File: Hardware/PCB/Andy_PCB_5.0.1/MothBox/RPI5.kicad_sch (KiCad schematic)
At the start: 4 parts, among them U4 RASPBERRY_PI_4B_4GB, U5 RASPBERRY_PI_5, U6 RASPBERRY_PI_4B_4GB, U7 Female Inv Socket Pi 2.54-2*20

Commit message: daily schematic updates
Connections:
- net +3.3V: now also U5.17 (3V3)
- net COM_I/O: no longer names the net of U7.35
- net EN_MUX1 renamed UV2_CTRL
- net EN_MUX2 renamed UV3_CTRL
- net L_LED_CTRL renamed PHOTO_LED_CTRL
- net S0_MUX: no longer names the net of U7.34
- net S1_MUX: no longer names the net of U7.14
- net S2_MUX: no longer names the net of U7.11
- net S3_MUX: no longer names the net of U7.16
- no-connect marks 20 -> 24

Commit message: updated photo LEDs and the power page
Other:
- company: (none) -> Digital Naturalism Laboritories
- title: (none) -> MothBox
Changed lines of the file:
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@@
 	(generator_version "9.0")
 	(paper "User" 381 254)
+	(title_block
+		(title "MothBox")
+		(date "2025-07-12")
+		(rev "5.0.1")
+		(company "Digital Naturalism Laboritories")
+	)
 	(rectangle
 		(start 19.05 16.51)

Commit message: updated footprints and schematic
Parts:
- U4, U6: symbol MB_Library:RASPBERRY_PI_4B_4GB_1 -> MothBox_Symbol_Library:RASPBERRY_PI_4B_4GB_1; Digikey Part No SC1113 -> (none); Digikey_Part_No (none) -> SC1113
- U5: symbol MB_Library:RASPBERRY_PI_4B_4GB_2 -> MothBox_Symbol_Library:RASPBERRY_PI_4B_4GB_2; LCSC Part no  C5224014 -> (none); LCSC_Part_No (none) -> C5224014
- U7: footprint easyeda2kicad:HDR-TH_40P-P2.54-H-F-R2-C20-W8.5 -> easyeda_footprints:HDR-TH_40P-P2.54-H-F-R2-C20-W8.5; symbol MB_Library:2.54-2*20 -> MothBox_Symbol_Library:2.54-2*20; LCSC Part C2897440 -> (none); LCSC_Part (none) -> C2897440
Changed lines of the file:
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@@
 	(symbol
 		(lib_name "RASPBERRY_PI_4B_4GB_1")
-		(lib_id "MB_Library:RASPBERRY_PI_4B_4GB_1")
+		(lib_id "MothBox_Symbol_Library:RASPBERRY_PI_4B_4GB_1")
 		(at 102.87 173.99 0)
 		(unit 1)
@@
 			)
 		)
-		(property "Digikey Part No" "SC1113"
-			(at 102.87 173.99 0)
-			(effects
-				(font
-					(size 1.27 1.27)
-				)
-				(justify bottom)
-				(hide yes)
-			)
-		)
 		(property "Availability" "Not in stock"
 			(at 102.87 173.99 0)
@@
 			)
 		)
-		(property "LCSC PN" ""
-			(at 102.87 173.99 0)
-			(effects
-				(font
-					(size 1.27 1.27)
-				)
+		(property "AVAILABILITY" ""
+			(at 102.87 173.99 0)
+			(effects
+				(font
+					(size 1.27 1.27)
+				)
+				(hide yes)
+			)
+		)
+		(property "DESCRIPTION" ""
+			(at 102.87 173.99 0)
+			(effects
+				(font
+					(size 1.27 1.27)
+				)
+				(hide yes)
+			)
+		)
+		(property "Link" ""
+			(at 102.87 173.99 0)
+			(effects
+				(font
+					(size 1.27 1.27)
+				)
+				(hide yes)
+			)
+		)
+		(property "PACKAGE" ""
+			(at 102.87 173.99 0)
+			(effects
+				(font
+					(size 1.27 1.27)
+				)
+				(hide yes)
+			)
+		)
+		(property "PRICE" ""
+			(at 102.87 173.99 0)
+			(effects
+				(font
+					(size 1.27 1.27)
+				)
+				(hide yes)
+			)
+		)
+		(property "Digikey_Part_No" "SC1113"
+			(at 102.87 173.99 0)
+			(effects
+				(font
+					(size 1.27 1.27)
+				)
+				(hide yes)
 			)
 		)
@@
 	)
 	(symbol
-		(lib_id "MB_Library:GND")
+		(lib_id "MothBox_Symbol_Library:GND")
 		(at 137.16 111.76 0)
 		(unit 1)
@@
 	)
 	(symbol
-		(lib_id "MB_Library:GND")
+		(lib_id "MothBox_Symbol_Library:GND")
 		(at 97.79 124.46 0)
 		(unit 1)
@@
 	)
 	(symbol
-		(lib_id "MB_Library:+5V")
+		(lib_id "MothBox_Symbol_Library:+5V")
 		(at 97.79 39.37 0)
 		(unit 1)
@@
 	(symbol
 		(lib_name "RASPBERRY_PI_4B_4GB_2")
-		(lib_id "MB_Library:RASPBERRY_PI_4B_4GB_2")
+		(lib_id "MothBox_Symbol_Library:RASPBERRY_PI_4B_4GB_2")
 		(at 71.12 71.12 0)
 		(unit 1)
@@
 			)
 		)
-		(property "LCSC Part no " "C5224014"
+		(property "AVAILABILITY" ""
+			(at 71.12 71.12 0)
+			(effects
+				(font
+					(size 1.27 1.27)
+				)
+				(hide yes)
+			)
+		)
+		(property "DESCRIPTION" ""
+			(at 71.12 71.12 0)
+			(effects
+				(font
+					(size 1.27 1.27)
+				)
+				(hide yes)
+			)
+		)
+		(property "Link" ""
+			(at 71.12 71.12 0)
+			(effects
+				(font
+					(size 1.27 1.27)
+				)
+				(hide yes)
+			)
+		)
+		(property "PACKAGE" ""
+			(at 71.12 71.12 0)
+			(effects
+				(font
+					(size 1.27 1.27)
+				)
+				(hide yes)
+			)
+		)
+		(property "PRICE" ""
+			(at 71.12 71.12 0)
+			(effects
+				(font
+					(size 1.27 1.27)
+				)
+				(hide yes)
+			)
+		)
+		(property "LCSC_Part_No" "C5224014"
 			(at 71.12 71.12 0)
 			(effects
@@
 	)
 	(symbol
-		(lib_id "MB_Library:+3.3V")
+		(lib_id "MothBox_Symbol_Library:+3.3V")
 		(at 100.33 46.99 0)
 		(unit 1)
@@
 	)
 	(symbol
-		(lib_id "MB_Library:GND")
+		(lib_id "MothBox_Symbol_Library:GND")
 		(at 213.36 102.87 0)
 		(unit 1)
@@
 	(symbol
 		(lib_name "RASPBERRY_PI_4B_4GB_1")
-		(lib_id "MB_Library:RASPBERRY_PI_4B_4GB_1")
+		(lib_id "MothBox_Symbol_Library:RASPBERRY_PI_4B_4GB_1")
 		(at 64.77 172.72 0)
 		(unit 1)
@@
 			)
 		)
-		(property "Digikey Part No" "SC1113"
-			(at 64.77 172.72 0)
-			(effects
-				(font
-					(size 1.27 1.27)
-				)
-				(justify bottom)
-				(hide yes)
-			)
-		)
 		(property "Availability" "Not in stock"
 			(at 64.77 172.72 0)
@@
 			)
 		)
-		(property "LCSC PN" ""
-			(at 64.77 172.72 0)
-			(effects
-				(font
-					(size 1.27 1.27)
-				)
+		(property "AVAILABILITY" ""
+			(at 64.77 172.72 0)
+			(effects
+				(font
+					(size 1.27 1.27)
+				)
+				(hide yes)
+			)
+		)
+		(property "DESCRIPTION" ""
+			(at 64.77 172.72 0)
+			(effects
+				(font
+					(size 1.27 1.27)
+				)
+				(hide yes)
+			)
+		)
+		(property "Link" ""
+			(at 64.77 172.72 0)
+			(effects
+				(font
+					(size 1.27 1.27)
+				)
+				(hide yes)
+			)
+		)
+		(property "PACKAGE" ""
+			(at 64.77 172.72 0)
+			(effects
+				(font
+					(size 1.27 1.27)
+				)
+				(hide yes)
+			)
+		)
+		(property "PRICE" ""
+			(at 64.77 172.72 0)
+			(effects
+				(font
+					(size 1.27 1.27)
+				)
+				(hide yes)
+			)
+		)
+		(property "Digikey_Part_No" "SC1113"
+			(at 64.77 172.72 0)
+			(effects
+				(font
+					(size 1.27 1.27)
+				)
+				(hide yes)
 			)
 		)
@@
 	)
 	(symbol
-		(lib_id "MB_Library:+5V")
+		(lib_id "MothBox_Symbol_Library:+5V")
 		(at 195.58 60.96 0)
 		(unit 1)
@@
 	)
 	(symbol
-		(lib_id "MB_Library:2.54-2*20")
+		(lib_id "MothBox_Symbol_Library:2.54-2*20")
 		(at 184.15 87.63 0)
 		(mirror y)
@@
 			)
 		)
-		(property "Footprint" "easyeda2kicad:HDR-TH_40P-P2.54-H-F-R2-C20-W8.5"
+		(property "Footprint" "easyeda_footprints:HDR-TH_40P-P2.54-H-F-R2-C20-W8.5"
 			(at 184.15 118.11 0)
 			(effects
@@
 			)
 		)
-		(property "LCSC Part" "C2897440"
-			(at 184.15 120.65 0)
+		(property "AVAILABILITY" ""
+			(at 184.15 87.63 0)
+			(effects
+				(font
+					(size 1.27 1.27)
+				)
+				(hide yes)
+			)
+		)
+		(property "DESCRIPTION" ""
+			(at 184.15 87.63 0)
+			(effects
+				(font
+					(size 1.27 1.27)
+				)
+				(hide yes)
+			)
+		)
+		(property "Link" ""
+			(at 184.15 87.63 0)
+			(effects
+				(font
+					(size 1.27 1.27)
+				)
+				(hide yes)
+			)
+		)
+		(property "PACKAGE" ""
+			(at 184.15 87.63 0)
+			(effects
+				(font
+					(size 1.27 1.27)
+				)
+				(hide yes)
+			)
+		)
+		(property "PRICE" ""
+			(at 184.15 87.63 0)
+			(effects
+				(font
+					(size 1.27 1.27)
+				)
+				(hide yes)
+			)
+		)
+		(property "LCSC_Part" "C2897440"
+			(at 184.15 87.63 0)
 			(effects
 				(font
@@
 	)
 	(symbol
-		(lib_id "MB_Library:+3.3V")
+		(lib_id "MothBox_Symbol_Library:+3.3V")
 		(at 172.72 62.23 0)
 		(unit 1)

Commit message: daily PCB update
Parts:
- U5: footprint AQLibrary:EPAPER_PinHeader_2x20_P2.54mm_Vertical -> MothBox_footprints_Library:EPAPER_PinHeader_2x20_P2.54mm_Vertical
- U7: footprint easyeda_footprints:HDR-TH_40P-P2.54-H-F-R2-C20-W8.5 -> MothBox_footprints_Library:HDR-TH_40P-P2.54-H-F-R2-C20-W8.5
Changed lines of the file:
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@@
+			)
+		)
+		(property "Ali_Express_Link" ""
+			(at 102.87 173.99 0)
+			(effects
+				(font
+					(size 1.27 1.27)
+				)
+				(hide yes)
+			)
+		)
+		(property "LCSC_PN" ""
+			(at 102.87 173.99 0)
+			(effects
+				(font
+					(size 1.27 1.27)
+				)
+				(hide yes)
 			)
 		)
@@
 			)
 		)
-		(property "Footprint" "AQLibrary:EPAPER_PinHeader_2x20_P2.54mm_Vertical"
+		(property "Footprint" "MothBox_footprints_Library:EPAPER_PinHeader_2x20_P2.54mm_Vertical"
 			(at 71.12 71.12 0)
 			(effects
@@
 		)
 		(property "LCSC_Part_No" "C5224014"
+			(at 71.12 71.12 0)
+			(effects
+				(font
+					(size 1.27 1.27)
+				)
+				(hide yes)
+			)
+		)
+		(property "Ali_Express_Link" ""
+			(at 71.12 71.12 0)
+			(effects
+				(font
+					(size 1.27 1.27)
+				)
+				(hide yes)
+			)
+		)
+		(property "LCSC_PN" ""
 			(at 71.12 71.12 0)
 			(effects
@@
 			)
 		)
+		(property "Ali_Express_Link" ""
+			(at 64.77 172.72 0)
+			(effects
+				(font
+					(size 1.27 1.27)
+				)
+				(hide yes)
+			)
+		)
+		(property "LCSC_PN" ""
+			(at 64.77 172.72 0)
+			(effects
+				(font
+					(size 1.27 1.27)
+				)
+				(hide yes)
+			)
+		)
 		(instances
 			(project ""
@@
 			)
 		)
-		(property "Footprint" "easyeda_footprints:HDR-TH_40P-P2.54-H-F-R2-C20-W8.5"
+		(property "Footprint" "MothBox_footprints_Library:HDR-TH_40P-P2.54-H-F-R2-C20-W8.5"
 			(at 184.15 118.11 0)
 			(effects
@@
 			(at 184.15 87.63 0)
 			(effects
+				(font
+					(size 1.27 1.27)
+				)
+				(hide yes)
+			)
+		)
+		(property "Ali_Express_Link" ""
+			(at 184.15 87.63 0)
+			(effects
+				(font
+					(size 1.27 1.27)
+				)
+				(hide yes)
+			)
+		)
+		(property "LCSC_PN" ""
+			(at 184.15 87.63 0)
+			(effects

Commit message: rough outline of PCB. Lots of tidying up needed
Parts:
- added TP7: 3V3_test, MothBox_footprints_Library:TestPoint_THTPad_D1.0mm_Drill0.5mm, symbol MothBox_Symbol_Library:TestPoint
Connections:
- net +3.3V: now also TP7.1
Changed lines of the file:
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@@
+	)
+	(junction
+		(at 100.33 48.26)
+		(diameter 0)
+		(color 0 0 0 0)
 	)
 	(junction
@@
 		(pts
 			(xy 96.52 43.18) (xy 97.79 43.18)
+		)
+		(stroke
+			(width 0)
+			(type default)
+		)
+	)
+	(wire
+		(pts
+			(xy 100.33 48.26) (xy 104.14 48.26)
 		)
 		(stroke
@@
 		)
 		(property "Value" "+3.3V"
-			(at 103.886 43.434 0)
+			(at 100.584 43.434 0)
 			(effects
 				(font
@@
 		(dnp no)
 		(property "Reference" "U7"
-			(at 179.832 57.912 0)
+			(at 184.15 58.166 0)
 			(effects
 				(font
@@
 				(path "/9021e528-fc76-4423-a3f3-30f5652071cc/23e8100d-dc92-4d1f-bb27-d65b0331e323"
 					(reference "U7")
+					(unit 1)
+				)
+			)
+		)
+	)
+	(symbol
+		(lib_id "MothBox_Symbol_Library:TestPoint")
+		(at 104.14 48.26 0)
+		(mirror y)
+		(unit 1)
+		(exclude_from_sim no)
+		(in_bom yes)
+		(on_board yes)
+		(dnp no)
+		(property "Reference" "TP7"
+			(at 107.442 46.482 0)
+			(effects
+				(font
+					(size 1.27 1.27)
+				)
+			)
+		)
+		(property "Value" "3V3_test"
+			(at 108.966 43.942 0)
+			(effects
+				(font
+					(size 1.27 1.27)
+				)
+			)
+		)
+		(property "Footprint" "MothBox_footprints_Library:TestPoint_THTPad_D1.0mm_Drill0.5mm"
+			(at 99.06 48.26 0)
+			(effects
+				(font
+					(size 1.27 1.27)
+				)
+				(hide yes)
+			)
+		)
+		(property "Datasheet" "~"
+			(at 99.06 48.26 0)
+			(effects
+				(font
+					(size 1.27 1.27)
+				)
+				(hide yes)
+			)
+		)
+		(property "Description" "test point"
+			(at 104.14 48.26 0)
+			(effects
+				(font
+					(size 1.27 1.27)
+				)
+				(hide yes)
+			)
+		)
+		(property "AVAILABILITY" ""
+			(at 104.14 48.26 0)
+			(effects
+				(font
+					(size 1.27 1.27)
+				)
+				(hide yes)
+			)
+		)
+		(property "DESCRIPTION" ""
+			(at 104.14 48.26 0)
+			(effects
+				(font
+					(size 1.27 1.27)
+				)
+				(hide yes)
+			)
+		)
+		(property "Link" ""
+			(at 104.14 48.26 0)
+			(effects
+				(font
+					(size 1.27 1.27)
+				)
+				(hide yes)
+			)
+		)
+		(property "PACKAGE" ""
+			(at 104.14 48.26 0)
+			(effects
+				(font
+					(size 1.27 1.27)
+				)
+				(hide yes)
+			)
+		)
+		(property "PRICE" ""
+			(at 104.14 48.26 0)
+			(effects
+				(font
+					(size 1.27 1.27)
+				)
+				(hide yes)
+			)
+		)
+		(property "Ali_Express_Link" ""
+			(at 104.14 48.26 0)
+			(effects
+				(font
+					(size 1.27 1.27)
+				)
+				(hide yes)
+			)
+		)
+		(property "LCSC_PN" ""
+			(at 104.14 48.26 0)
+			(effects
+				(font
+					(size 1.27 1.27)
+				)
+				(hide yes)
+			)
+		)
+		(pin "1"
+		)
+		(instances
+			(project "MothBox"
+				(path "/9021e528-fc76-4423-a3f3-30f5652071cc/23e8100d-dc92-4d1f-bb27-d65b0331e323"
+					(reference "TP7")
 					(unit 1)
 				)
@@
 		)
 		(property "Value" "+3.3V"
-			(at 169.164 58.928 0)
-			(effects
-				(font
+			(at 173.99 58.42 0)
+			(effects
+				(font

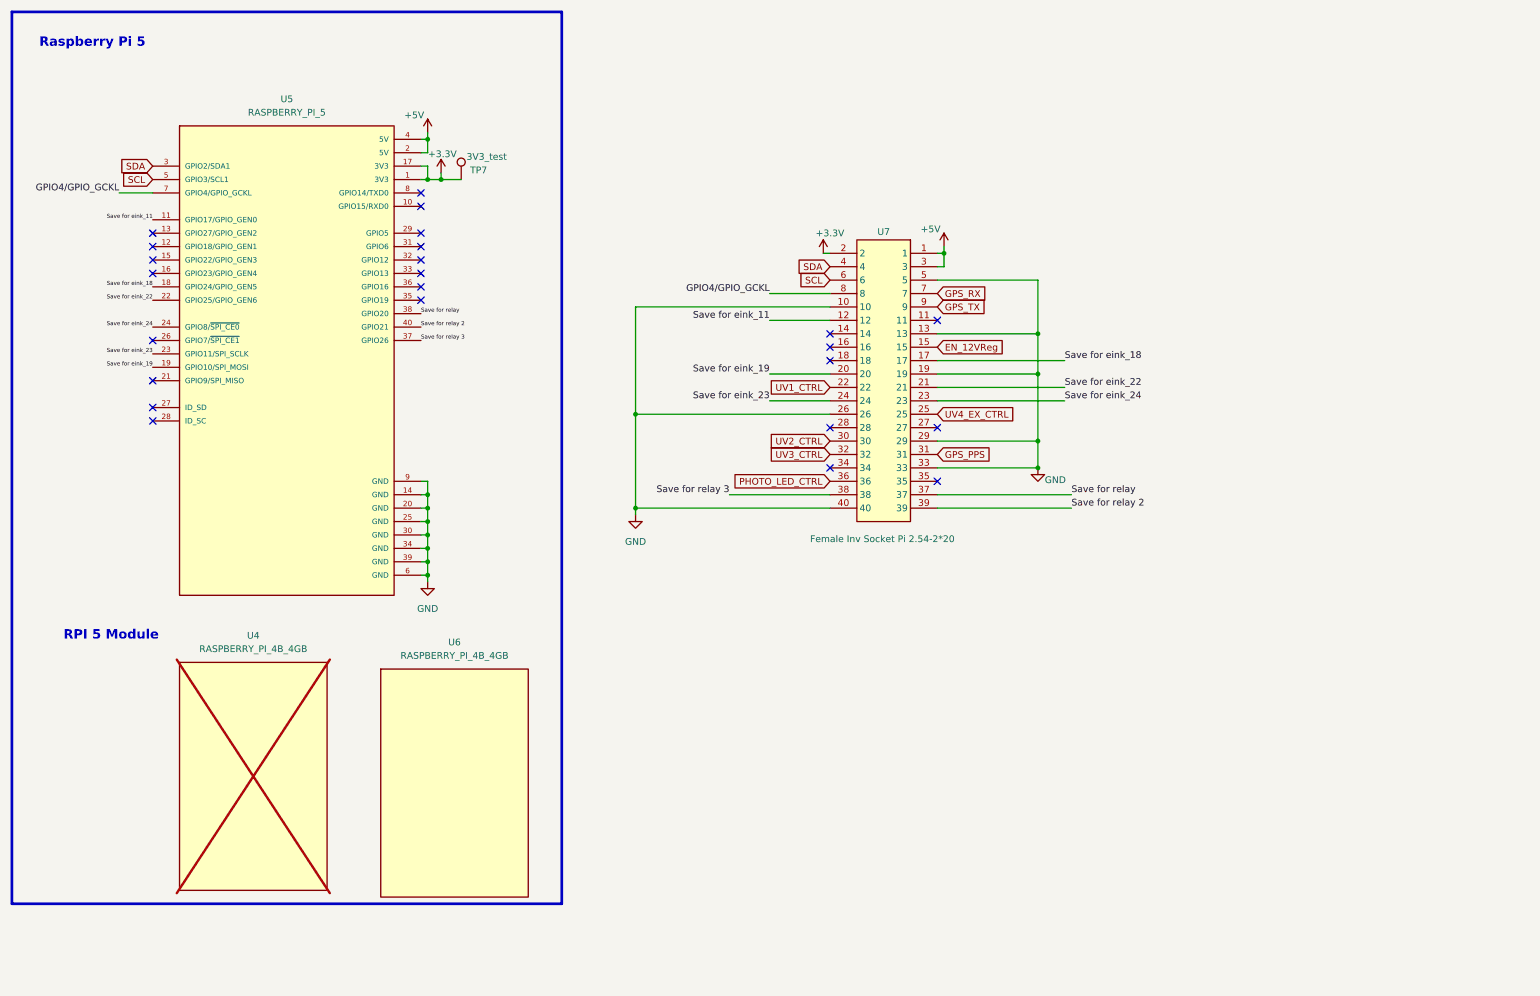
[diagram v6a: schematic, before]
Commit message: updated MothBeam PCB Edge and MothBox PCB
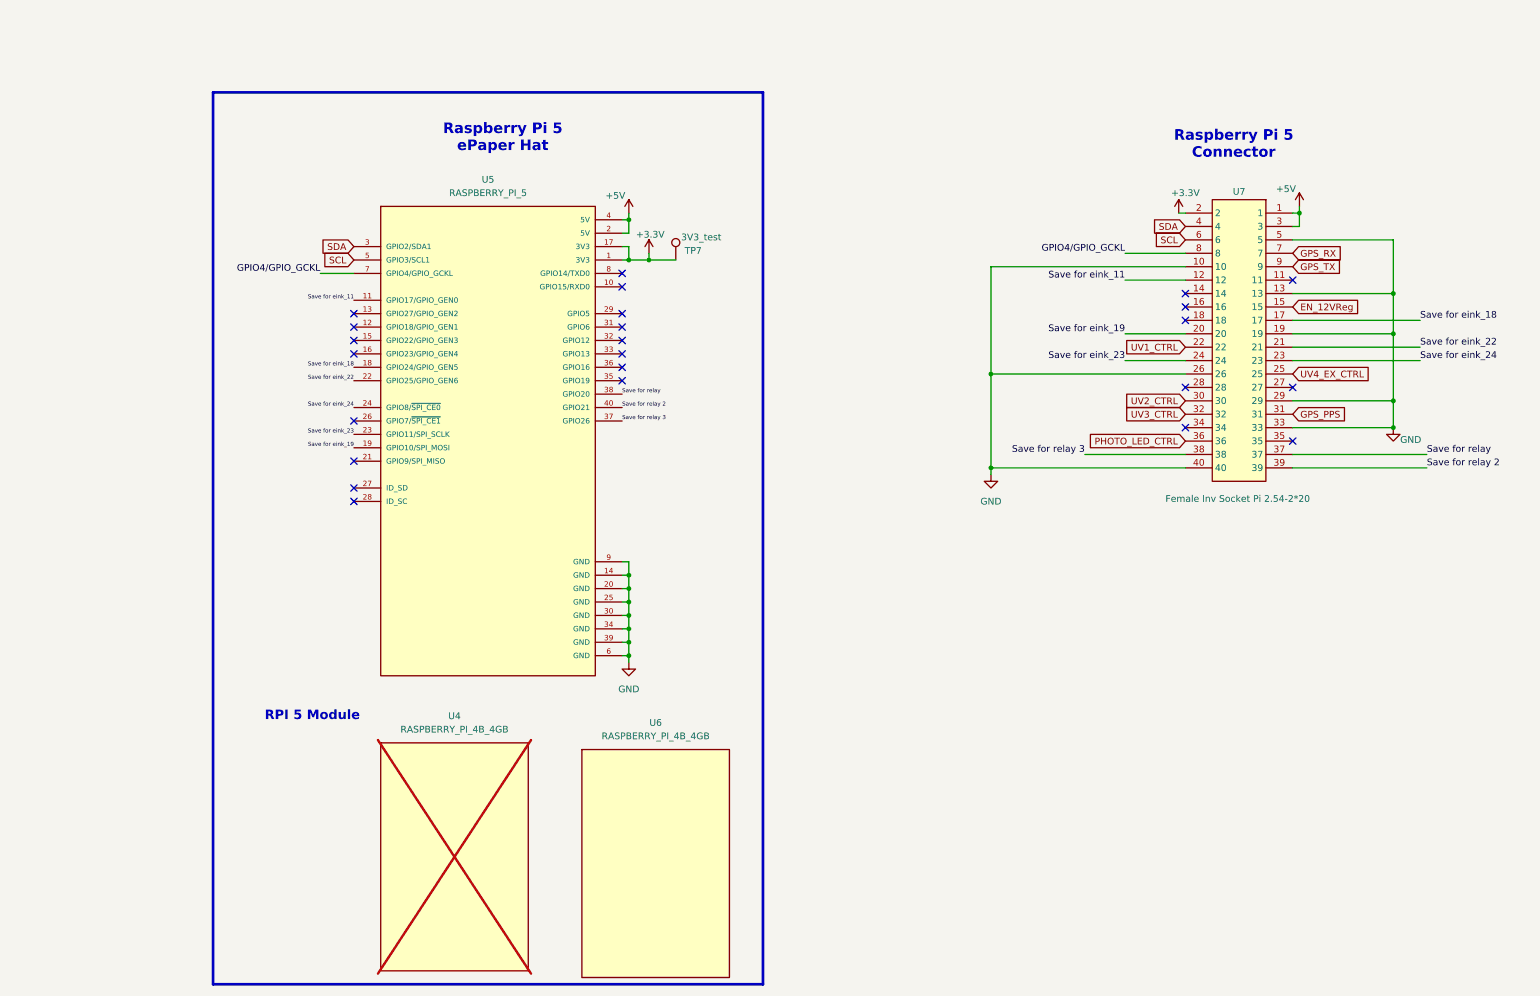
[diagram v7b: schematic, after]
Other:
- note added: "Raspberry Pi 5 Connector"
- note added: "Raspberry Pi 5 ePaper Hat"
- note removed: "Raspberry Pi 5"
- moved on the sheet: TP7, U4, U5, U6, U7

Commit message: added in extra hour switch for 24hr coverage
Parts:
- TP7: now left out of the parts list
- U5: LCSC_Part (none) -> C5224014; LCSC_Part_No C5224014 -> (none)
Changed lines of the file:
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@@
+			)
+		)
+		(property "Sim.Device" ""
+			(at 140.97 189.23 0)
+			(effects
+				(font
+					(size 1.27 1.27)
+				)
+				(hide yes)
+			)
+		)
+		(property "Sim.Pins" ""
+			(at 140.97 189.23 0)
+			(effects
+				(font
+					(size 1.27 1.27)
+				)
+				(hide yes)
+			)
+		)
+		(property "Sim.Type" ""
+			(at 140.97 189.23 0)
+			(effects
+				(font
+					(size 1.27 1.27)
+				)
+				(hide yes)
 			)
 		)
@@
 			)
 		)
-		(property "LCSC_Part_No" "C5224014"
+		(property "LCSC_Part_No" ""
 			(at 109.22 86.36 0)
 			(effects
@@
 		)
 		(property "LCSC_PN" ""
+			(at 109.22 86.36 0)
+			(effects
+				(font
+					(size 1.27 1.27)
+				)
+				(hide yes)
+			)
+		)
+		(property "LCSC_Part" "C5224014"
+			(at 109.22 86.36 0)
+			(effects
+				(font
+					(size 1.27 1.27)
+				)
+				(hide yes)
+			)
+		)
+		(property "Sim.Device" ""
+			(at 109.22 86.36 0)
+			(effects
+				(font
+					(size 1.27 1.27)
+				)
+				(hide yes)
+			)
+		)
+		(property "Sim.Pins" ""
+			(at 109.22 86.36 0)
+			(effects
+				(font
+					(size 1.27 1.27)
+				)
+				(hide yes)
+			)
+		)
+		(property "Sim.Type" ""
 			(at 109.22 86.36 0)
 			(effects
@@
 			)
 		)
+		(property "Sim.Device" ""
+			(at 102.87 187.96 0)
+			(effects
+				(font
+					(size 1.27 1.27)
+				)
+				(hide yes)
+			)
+		)
+		(property "Sim.Pins" ""
+			(at 102.87 187.96 0)
+			(effects
+				(font
+					(size 1.27 1.27)
+				)
+				(hide yes)
+			)
+		)
+		(property "Sim.Type" ""
+			(at 102.87 187.96 0)
+			(effects
+				(font
+					(size 1.27 1.27)
+				)
+				(hide yes)
+			)
+		)
 		(instances
 			(project ""
@@
 			)
 		)
+		(property "Sim.Device" ""
+			(at 251.46 80.01 0)
+			(effects
+				(font
+					(size 1.27 1.27)
+				)
+				(hide yes)
+			)
+		)
+		(property "Sim.Pins" ""
+			(at 251.46 80.01 0)
+			(effects
+				(font
+					(size 1.27 1.27)
+				)
+				(hide yes)
+			)
+		)
+		(property "Sim.Type" ""
+			(at 251.46 80.01 0)
+			(effects
+				(font
+					(size 1.27 1.27)
+				)
+				(hide yes)
+			)
+		)
 		(pin "13"
 		)
@@
 		(unit 1)
 		(exclude_from_sim no)
-		(in_bom yes)
+		(in_bom no)
 		(on_board yes)
 		(dnp no)
@@
 			(at 144.78 63.5 0)
 			(effects
+				(font
+					(size 1.27 1.27)
+				)
+				(hide yes)
+			)
+		)
+		(property "Sim.Device" ""
+			(at 144.78 63.5 0)
+			(effects
+				(font
+					(size 1.27 1.27)
+				)
+				(hide yes)
+			)
+		)
+		(property "Sim.Pins" ""
+			(at 144.78 63.5 0)
+			(effects
+				(font
+					(size 1.27 1.27)
+				)
+				(hide yes)
+			)
+		)
+		(property "Sim.Type" ""
+			(at 144.78 63.5 0)
+			(effects
